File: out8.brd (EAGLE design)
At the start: 100 x 80 mm, 30 parts, among them IC104 74HC594N, K301 S202S02, K302 S202S02, K303 S202S02, K304 S202S02, K305 S202S02, K306 S202S02, K307 S202S02, K308 S202S02

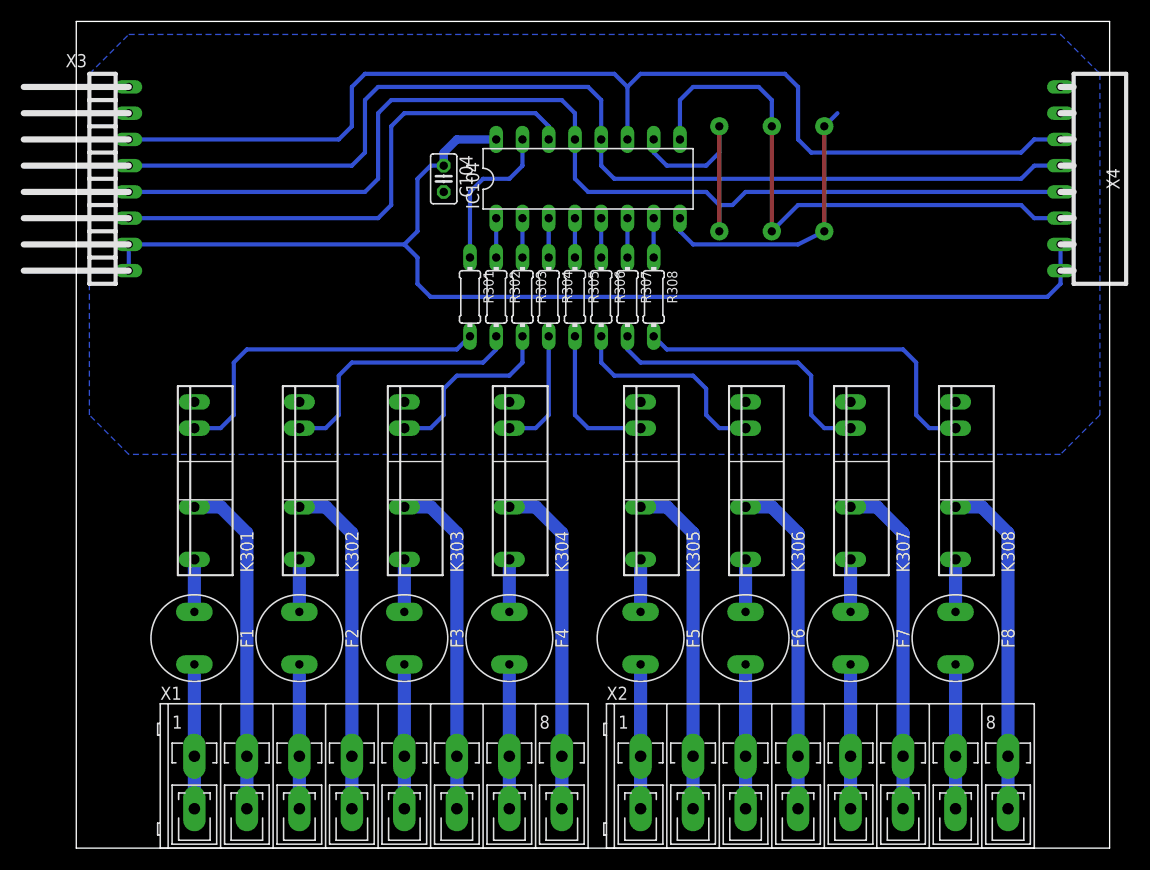
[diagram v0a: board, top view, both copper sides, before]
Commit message: LEDs auf Ausgangsplatine hinzugefügt
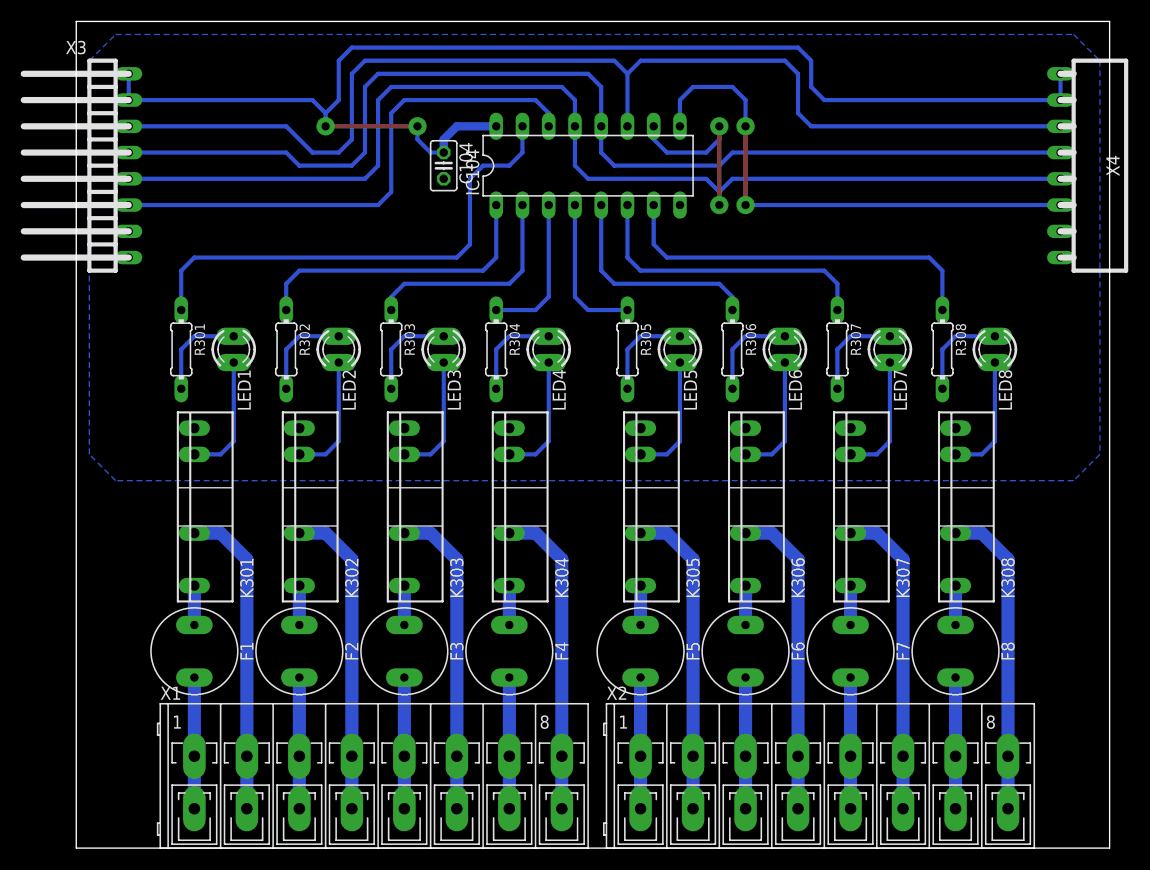
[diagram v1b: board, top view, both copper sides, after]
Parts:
- added LED1, LED2, LED3, LED4, LED5, LED6, LED7, LED8: (no value), led:LED3MM
- moved R301 28.4 mm to (10.2, 48.3)
- moved R308 28.4 mm to (83.8, 48.3)
- moved R302 20.9 mm to (20.3, 48.3)
- moved R307 20.9 mm to (73.7, 48.3)
- moved R306 13.7 mm to (63.5, 48.3)
- moved R303 13.7 mm to (30.5, 48.3)
- moved R305 7.18 mm to (53.3, 48.3)
- moved R304 7.18 mm to (40.6, 48.3)
- moved K301 2.54 mm to (11.4, 33.0)
- moved K302 2.54 mm to (21.6, 33.0)
- moved K303 2.54 mm to (31.8, 33.0)
- moved K304 2.54 mm to (41.9, 33.0)
- moved K305 2.54 mm to (54.6, 33.0)
- moved K306 2.54 mm to (64.8, 33.0)
- moved K307 2.54 mm to (74.9, 33.0)
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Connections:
- new net N$42: LED1.A, R301.2
- new net N$43: LED2.A, R302.2
- new net N$44: LED3.A, R303.2
- new net N$45: LED4.A, R304.2
- new net N$46: LED5.A, R305.2
- new net N$47: LED6.A, R306.2
- new net N$48: LED7.A, R307.2
- new net N$49: LED8.A, R308.2
- net +5V: now also X3.1, X3.2, X4.1, X4.2; no longer X3.7, X3.8, X4.7, X4.8
- net GND: now also X3.7, X3.8, X4.7, X4.8; no longer X3.1, X3.2, X4.1, X4.2
- net N$17: now also LED1.K; no longer R301.2
- net N$18: now also LED2.K; no longer R302.2
- net N$19: now also LED3.K; no longer R303.2
- net N$20: now also LED4.K; no longer R304.2
- net N$21: now also LED5.K; no longer R305.2
- net N$22: now also LED6.K; no longer R306.2
- net N$23: now also LED7.K; no longer R307.2
- net N$24: now also LED8.K; no longer R308.2
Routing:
- net N$1: track 15.0 -> 47.8 mm
- net N$8: track 3.81 -> 36.6 mm
- net GND: track 28.0 -> 0.00 mm, vias 2 -> 0
- net N$2: track 3.81 -> 29.0 mm
- net N$7: track 3.81 -> 29.0 mm
- net N$24: track 35.9 -> 12.0 mm
- net N$17: track 33.3 -> 12.0 mm
- net N$6: track 3.81 -> 21.4 mm
- net N$3: track 3.81 -> 21.4 mm
- net N$23: track 28.2 -> 12.0 mm
- net N$18: track 25.7 -> 12.0 mm
- net N$5: track 3.81 -> 14.5 mm
- net N$4: track 3.81 -> 14.5 mm
- net N$49: track 0.00 -> 9.42 mm
- net N$44: track 0.00 -> 9.42 mm
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
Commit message: Busstecker auf Ausgangsboard ersetzt; kleinere Layoutanpassungen
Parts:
- removed C104: 10nF, passiv:C025-025X050
- removed IC104: 74HC594N, 74xx-eu:DIL16
- removed X3: (no value), anschluss:STG8
- removed X4: (no value), anschluss:BUG8
- added C101: 10nF, passiv:C025-025X050
- added IC101: 74HC594N, 74xx-eu:DIL16
- added X101, X102: (no value), anschluss:WS16V
- moved LED3 5.08 mm to (30.5, 48.3)
- moved R303 5.08 mm to (35.6, 48.3)
- moved LED1 5.08 mm to (10.2, 48.3)
- moved R301 5.08 mm to (15.2, 48.3)
- moved LED2 5.08 mm to (20.3, 48.3)
- moved LED4 5.08 mm to (40.6, 48.3)
- moved R302 5.08 mm to (25.4, 48.3)
- moved R304 5.08 mm to (45.7, 48.3)
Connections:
- net !R: now also IC101.10, IC101.13, X101.10, X101.9, X102.10, X102.9; no longer IC104.10, IC104.13, X3.5, X4.5
- net +5V: now also C101.1, IC101.16, X101.1, X101.2, X101.3, X101.4, X102.1, X102.2, X102.3, X102.4; no longer C104.1, IC104.16, X3.1, X3.2, X4.1, X4.2
- net C1: now also IC101.11, X101.5, X101.6, X102.5, X102.6; no longer IC104.11, X3.3, X4.3
- net C2: now also IC101.12, X101.7, X101.8, X102.7, X102.8; no longer IC104.12, X3.4, X4.4
- net D: now also IC101.14, X101.11, X101.12; no longer IC104.14, X3.6
- net GND: now also C101.2, IC101.8, X101.13, X101.14, X101.15, X101.16, X102.13, X102.14, X102.15, X102.16; no longer C104.2, IC104.8, X3.7, X3.8, X4.7, X4.8
- net N$1: now also IC101.15; no longer IC104.15
- net N$2: now also IC101.1; no longer IC104.1
- net N$3: now also IC101.2; no longer IC104.2
- net N$4: now also IC101.3; no longer IC104.3
- net N$41: now also IC101.9, X102.11, X102.12; no longer IC104.9, X4.6
- net N$5: now also IC101.4; no longer IC104.4
- net N$6: now also IC101.5; no longer IC104.5
- net N$7: now also IC101.6; no longer IC104.6
- net N$8: now also IC101.7; no longer IC104.7
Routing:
- net +5V: track 125.6 -> 130.7 mm
- net N$41: track 50.6 -> 45.5 mm
- net N$6: track 21.4 -> 18.8 mm
- net N$2: track 29.0 -> 26.5 mm
- net N$7: track 29.0 -> 26.5 mm
- net N$5: track 14.5 -> 12.0 mm
- net N$4: track 14.5 -> 12.0 mm
- net N$3: track 21.4 -> 18.8 mm
- net N$1: track 47.8 -> 45.3 mm
- net N$8: track 36.6 -> 34.1 mm
- net D: track 51.1 -> 53.6 mm
- net N$20: track 12.0 -> 11.2 mm
- net N$47: track 9.42 -> 8.67 mm
- net N$19: track 12.0 -> 11.2 mm
- net N$17: track 12.0 -> 11.2 mm
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
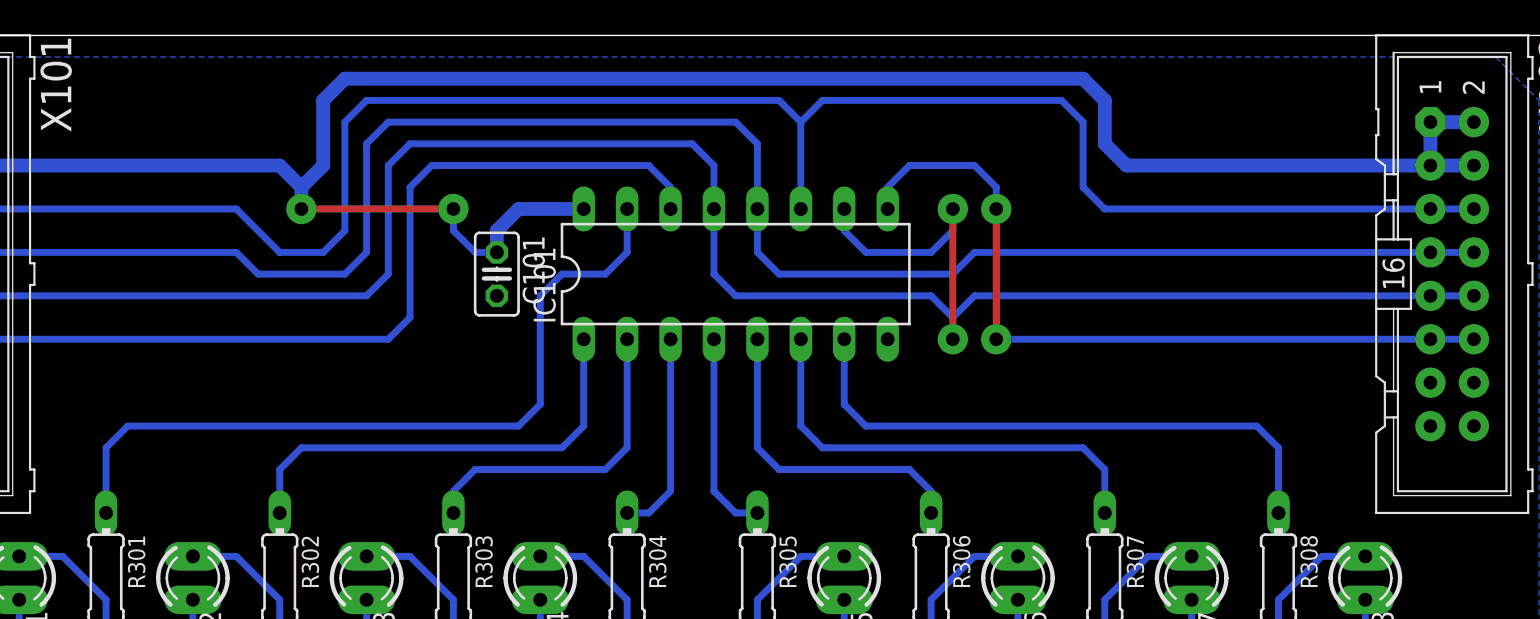
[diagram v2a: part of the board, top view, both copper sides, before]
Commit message: Dipschalter durch Drehschalter ersetzt; 74HC594 durch 74HC595 ersetzt; Signalleitungen gedreht.
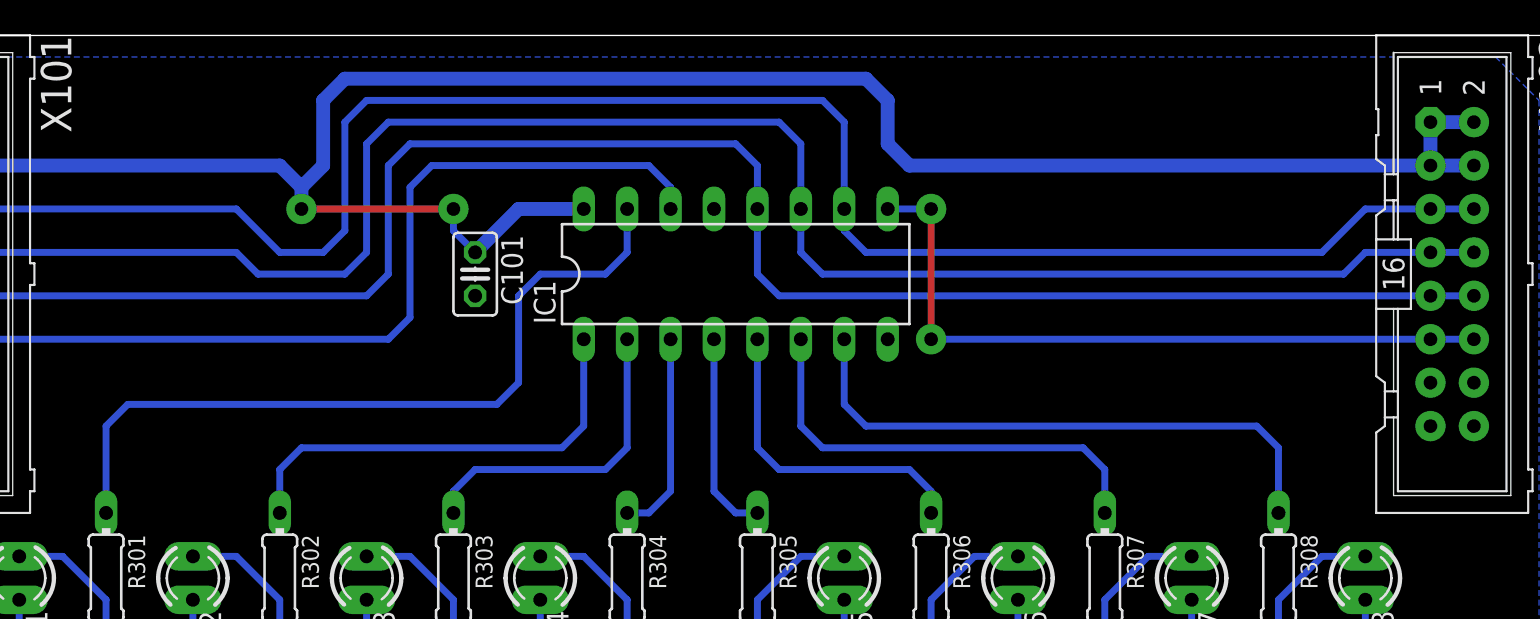
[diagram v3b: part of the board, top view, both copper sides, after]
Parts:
- IC1: value 74HC594N -> 74HC595N
- moved C101 1.27 mm to (36.8, 66.0)
- renumbered IC101 to IC1
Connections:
- net !R: now also X101.5, X101.6, X102.5, X102.6; no longer IC1.13, X101.10, X101.9, X102.10, X102.9
- net C1: now also X101.7, X101.8, X102.7, X102.8; no longer X101.5, X101.6, X102.5, X102.6
- net C2: now also X101.10, X101.9, X102.10, X102.9; no longer X101.7, X101.8, X102.7, X102.8
- net GND: now also IC1.13
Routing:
- net !R: track 124.9 -> 107.1 mm, vias 2 -> 0
- net C1: track 109.6 -> 106.0 mm
- net N$41: track 45.5 -> 41.9 mm
- net C2: track 106.0 -> 105.0 mm
- net +5V: track 130.7 -> 129.9 mm
